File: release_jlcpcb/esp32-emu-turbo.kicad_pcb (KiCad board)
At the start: 4 copper layers, 160 x 75 mm, 71 parts, among them J1 USB-C-16P, J3 JST-PH-2P, J4 FPC-40P-0.5mm, SW1 SW-SMD-5.1x5.1, SW10 SW-SMD-5.1x5.1, SW11 SW-SMD-5.1x5.1, SW12 SW-SMD-5.1x5.1, SW13 SW-SMD-5.1x5.1, SW2 SW-SMD-5.1x5.1, SW3 SW-SMD-5.1x5.1, SW4 SW-SMD-5.1x5.1, SW5 SW-SMD-5.1x5.1, SW6 SW-SMD-5.1x5.1, SW7 SW-SMD-5.1x5.1, SW8 SW-SMD-5.1x5.1, SW9 SW-SMD-5.1x5.1, U1 ESP32-S3-WROOM-1-N16R8, U2 ESOP-8, U3 SOT-223, U5 SOP-16, U6 TF-01A

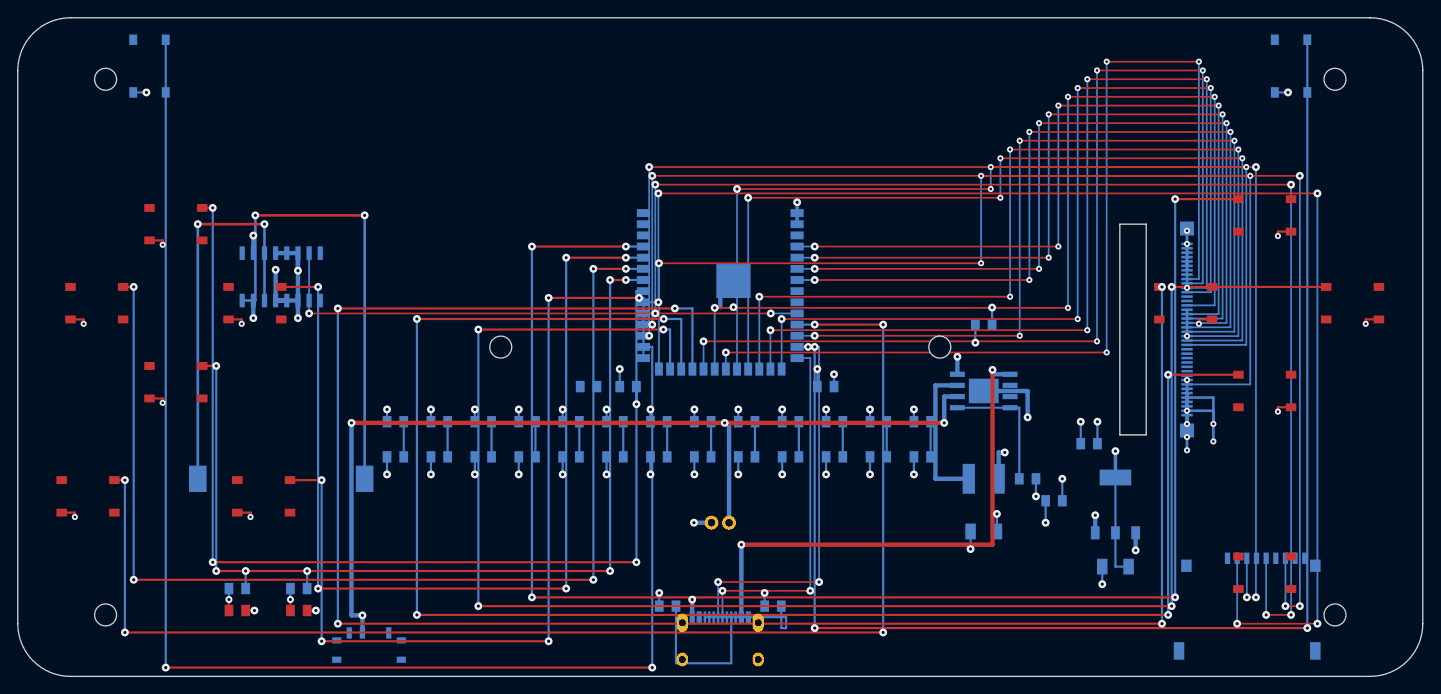
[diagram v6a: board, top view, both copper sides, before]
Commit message: Add JLCPCB DFM prevention: drill-trace + pad-net checks, pre-commit hook
Prevents two JLCPCB manufacturing review errors:
1. "The indicated hole will cut off the trace" — new drill-trace clearance test
2. "The pad and trace is connected" — pad net injection + trace-pad clearance test

Changes:
- routing.py: auto-capture pad-net mapping via _seg()/_via_net() endpoint matching
- board.py: inject correct net IDs into footprint pads (was net=0 for all)
- verify_dfm_v2.py: add _point_to_segment_dist(), test_drill_trace_clearance (42),
  test_trace_pad_different_net_clearance (43) with regression baselines
- pcb_cache.py: fix via net parsing regex (was broken, all vias showed net=0)
- drc_native.py: remove "shorting_items" from KNOWN_ACCEPTABLE (no longer needed)
- .git/hooks/pre-commit: run DFM verification on PCB file commits
- Regenerated PCB + gerbers + release_jlcpcb/ (43/43 DFM + 9/9 DFA pass)

Co-Authored-By: Claude Opus 4.6 <noreply@anthropic.com>
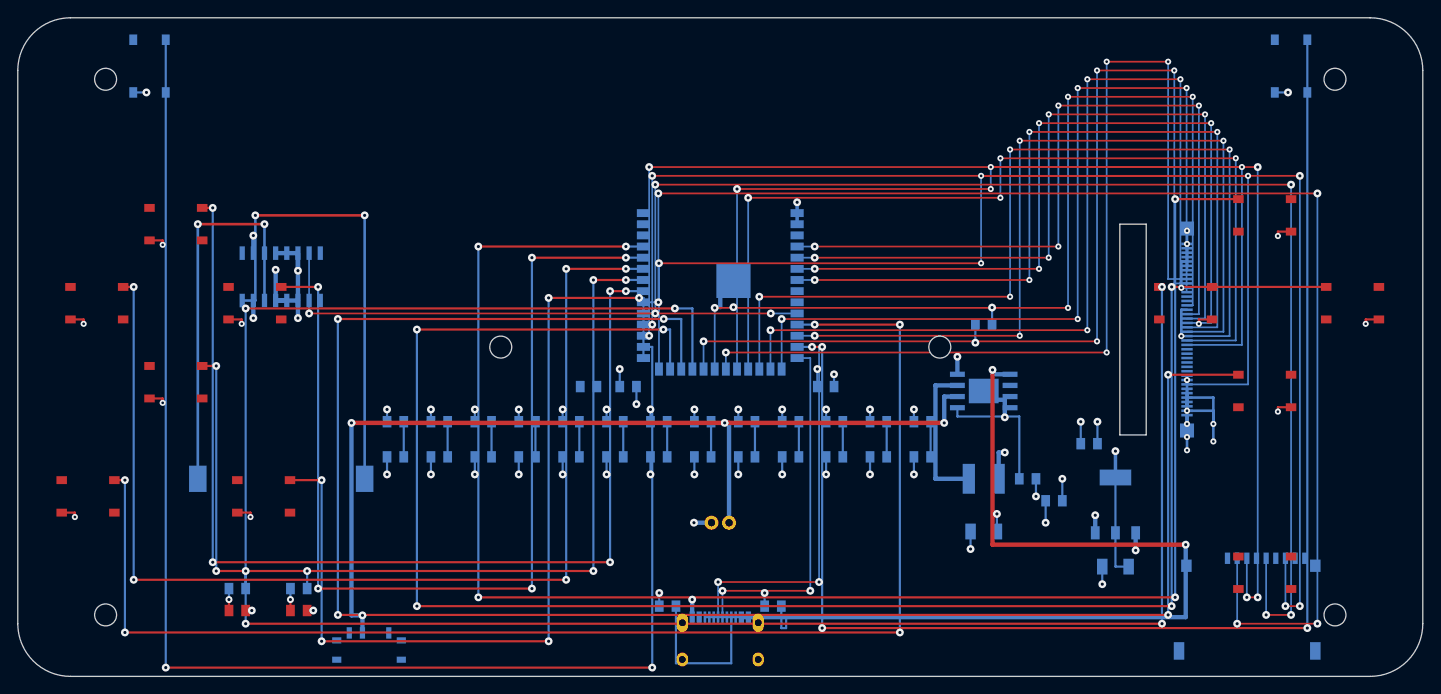
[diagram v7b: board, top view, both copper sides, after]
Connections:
- C1 pad 1: (no net) -> +5V
- C1 pad 2: (no net) -> GND
- C17 pad 1: (no net) -> VBUS
- C17 pad 2: (no net) -> GND
- C18 pad 1: (no net) -> BAT+
- C18 pad 2: (no net) -> GND
- C19 pad 1: (no net) -> +5V
- C19 pad 2: (no net) -> GND
- C2 pad 1: (no net) -> +3V3
- C2 pad 2: (no net) -> GND
- C3 pad 1: (no net) -> +3V3
- C3 pad 2: (no net) -> GND
- C4 pad 1: (no net) -> +3V3
- C4 pad 2: (no net) -> GND
- J1 pad A12: (no net) -> GND
- J1 pad A4: (no net) -> VBUS
- J1 pad A5: (no net) -> USB_CC1
- J1 pad A6: (no net) -> USB_D+
- J1 pad A7: (no net) -> USB_D-
- J1 pad B5: (no net) -> USB_CC2
- J3 pad 1: (no net) -> BAT+
- J3 pad 2: (no net) -> GND
- J4 pad 1: (no net) -> +3V3
- J4 pad 10: (no net) -> LCD_DC
- J4 pad 11: (no net) -> LCD_WR
- J4 pad 12: (no net) -> LCD_RD
- J4 pad 15: (no net) -> LCD_RST
- J4 pad 16: (no net) -> GND
- J4 pad 17: (no net) -> LCD_D0
- J4 pad 18: (no net) -> LCD_D1
- J4 pad 19: (no net) -> LCD_D2
- J4 pad 20: (no net) -> LCD_D3
- J4 pad 21: (no net) -> LCD_D4
- J4 pad 22: (no net) -> LCD_D5
- J4 pad 23: (no net) -> LCD_D6
- J4 pad 24: (no net) -> LCD_D7
- J4 pad 32: (no net) -> +3V3
- J4 pad 33: (no net) -> LCD_BL
- J4 pad 34: (no net) -> GND
- J4 pad 35: (no net) -> GND
- J4 pad 36: (no net) -> GND
- J4 pad 37: (no net) -> GND
- J4 pad 38: (no net) -> +3V3
- J4 pad 39: (no net) -> +3V3
- J4 pad 40: (no net) -> GND
- J4 pad 5: (no net) -> GND
- J4 pad 6: (no net) -> +3V3
- J4 pad 7: (no net) -> +3V3
- J4 pad 9: (no net) -> LCD_CS
- L1 pad 1: (no net) -> BAT+
- L1 pad 2: (no net) -> LX
- LED1 pad 2: (no net) -> GND
- LED2 pad 2: (no net) -> GND
- R1 pad 1: (no net) -> USB_CC1
- R1 pad 2: (no net) -> GND
- R16 pad 1: (no net) -> +5V
- R16 pad 2: (no net) -> IP5306_KEY
- R17 pad 1: (no net) -> +3V3
- R18 pad 1: (no net) -> +3V3
- R2 pad 1: (no net) -> USB_CC2
- R2 pad 2: (no net) -> GND
- SPK1 pad 1: (no net) -> SPK+
- SPK1 pad 2: (no net) -> SPK-
- SW1 pad 2: (no net) -> BTN_UP
- SW1 pad 3: (no net) -> GND
- SW10 pad 2: (no net) -> BTN_SELECT
- SW10 pad 3: (no net) -> GND
- SW11 pad 2: (no net) -> GND
- SW11 pad 3: (no net) -> BTN_L
- SW12 pad 2: (no net) -> GND
- SW12 pad 3: (no net) -> BTN_R
- SW2 pad 2: (no net) -> BTN_DOWN
- SW2 pad 3: (no net) -> GND
- SW3 pad 2: (no net) -> BTN_LEFT
- SW3 pad 3: (no net) -> GND
- SW4 pad 2: (no net) -> BTN_RIGHT
- SW4 pad 3: (no net) -> GND
- SW5 pad 1: (no net) -> BTN_A
- SW5 pad 4: (no net) -> GND
- SW6 pad 1: (no net) -> BTN_B
- SW6 pad 4: (no net) -> GND
- SW7 pad 1: (no net) -> BTN_X
- SW7 pad 4: (no net) -> GND
- SW8 pad 1: (no net) -> BTN_Y
- SW8 pad 4: (no net) -> GND
- SW9 pad 2: (no net) -> BTN_START
- SW9 pad 3: (no net) -> GND
- SW_PWR pad 2: (no net) -> BAT+
- U1 pad 10: (no net) -> I2S_DOUT
- U1 pad 11: (no net) -> BTN_START
- U1 pad 12: (no net) -> LCD_D4
- U1 pad 13: (no net) -> BTN_R
- U1 pad 14: (no net) -> USB_D+
- U1 pad 15: (no net) -> LCD_RD
- U1 pad 16: (no net) -> LCD_WR
- U1 pad 17: (no net) -> LCD_D5
- U1 pad 18: (no net) -> LCD_D6
- U1 pad 19: (no net) -> LCD_D7
- U1 pad 2: (no net) -> +3V3
- U1 pad 20: (no net) -> LCD_CS
- U1 pad 21: (no net) -> LCD_RST
- U1 pad 22: (no net) -> LCD_DC
- U1 pad 23: (no net) -> BTN_Y
- U1 pad 24: (no net) -> BTN_X
- U1 pad 25: (no net) -> BTN_B
- U1 pad 26: (no net) -> LCD_BL
- U1 pad 27: (no net) -> BTN_SELECT
- U1 pad 28: (no net) -> BTN_L
- U1 pad 29: (no net) -> SD_MOSI
- U1 pad 30: (no net) -> SD_MISO
- U1 pad 31: (no net) -> SD_CLK
- U1 pad 32: (no net) -> SD_CS
- U1 pad 33: (no net) -> BTN_UP
- U1 pad 34: (no net) -> BTN_DOWN
- U1 pad 35: (no net) -> BTN_LEFT
- U1 pad 36: (no net) -> BTN_RIGHT
- U1 pad 37: (no net) -> BTN_A
- U1 pad 4: (no net) -> LCD_D0
- U1 pad 41: (no net) -> GND
- U1 pad 5: (no net) -> LCD_D1
- U1 pad 6: (no net) -> LCD_D2
- U1 pad 7: (no net) -> LCD_D3
- U2 pad 1: (no net) -> VBUS
- U2 pad 5: (no net) -> IP5306_KEY
- U2 pad 6: (no net) -> BAT+
- U2 pad 7: (no net) -> LX
- U2 pad 8: (no net) -> +5V
- U2 pad EP: (no net) -> GND
- U3 pad 1: (no net) -> GND
- U3 pad 3: (no net) -> +5V
- U3 pad 4: (no net) -> +3V3
- U5 pad 10: (no net) -> I2S_DOUT
- U5 pad 11: (no net) -> GND
- U5 pad 12: (no net) -> +5V
- U5 pad 13: (no net) -> +5V
- U5 pad 14: (no net) -> SPK-
- U5 pad 15: (no net) -> GND
- U5 pad 16: (no net) -> SPK+
- U5 pad 2: (no net) -> GND
- U5 pad 4: (no net) -> +5V
- U5 pad 5: (no net) -> +5V
- U5 pad 6: (no net) -> +5V
- U5 pad 7: (no net) -> I2S_DOUT
- U6 pad 2: (no net) -> SD_CS
- U6 pad 3: (no net) -> SD_MOSI
- U6 pad 5: (no net) -> SD_CLK
- U6 pad 7: (no net) -> SD_MISO
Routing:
- net VBUS: track 61.3 -> 105.3 mm
- net BTN_Y: track 219.7 -> 240.7 mm
- net BTN_X: track 194.4 -> 212.4 mm
- net BTN_B: track 194.7 -> 208.7 mm
- net BTN_A: track 182.5 -> 194.7 mm
- net LCD_RD: track 106.8 -> 101.4 mm
- net LCD_RST: track 114.8 -> 109.8 mm
- net LCD_WR: track 108.7 -> 104.2 mm
- net LCD_D0: track 91.4 -> 86.9 mm
- net LCD_D1: track 92.1 -> 88.1 mm
- net BTN_START: track 153.8 -> 157.6 mm
- net LCD_DC: track 116.9 -> 113.3 mm
- net LCD_D2: track 92.7 -> 89.2 mm
- net LCD_D3: track 93.4 -> 90.4 mm
- net LCD_CS: track 115.0 -> 112.3 mm
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
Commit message: Fix PAM8403 copper-to-copper clearance violations, tighten DFM baselines
Routing fixes (routing.py):
- SPK+ (net42) exit U5:16 LEFTWARD (col_x=24.5) instead of right (+1.5mm).
  Old route at x=27.055 passed through U5:15 (GND pad, gap=-0.65mm) and
  U5:2 (GND pad, gap=-0.22mm). New route clears all U5 pads by >=0.605mm.
- Replace +5V bridge (VDD6→PVDD13 via x=31.905) with direct PVDD4→PVDD13
  vertical (x=29.365). Old bridge crossed U5:11 GND pad (gap=-0.45mm).
  New vert only touches same-net (+5V) pads U5:4 and U5:13.

Result: 157 -> 147 collision grid violations (-10). 43/43 DFM tests pass.

DFM baseline updates (verify_dfm_v2.py):
- Trace-to-pad baseline: 140 -> 106 (reflecting actual cleared violations)
- Drill-to-trace baseline: 71 -> 45

Release: gerbers, BOM, CPL, .kicad_pcb updated in release_jlcpcb/.

Co-Authored-By: Claude Opus 4.6 <noreply@anthropic.com>
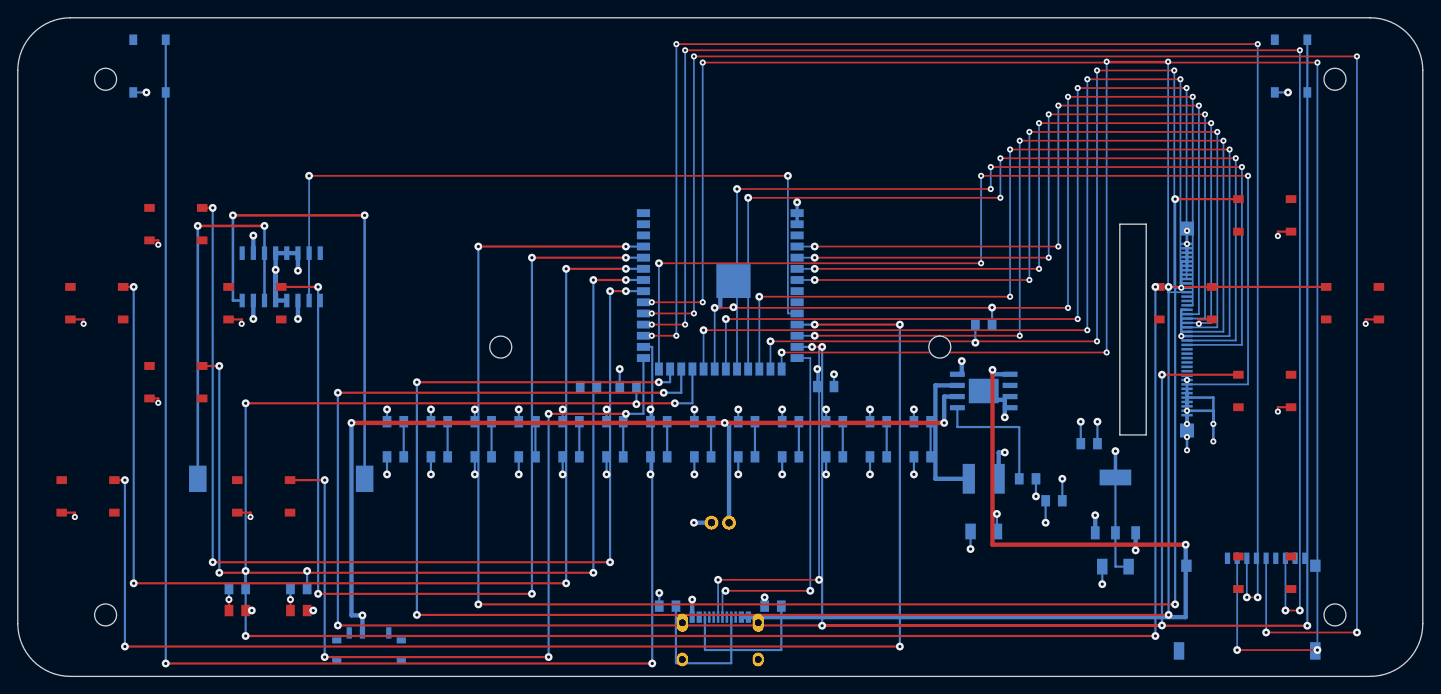
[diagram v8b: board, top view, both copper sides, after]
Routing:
- net SD_CLK: track 146.7 -> 194.9 mm, vias 5 -> 6
- net SD_CS: track 154.7 -> 190.5 mm, vias 5 -> 6
- net SD_MISO: track 147.8 -> 177.4 mm, vias 5 -> 6
- net I2S_DOUT: track 62.4 -> 90.8 mm
- net SD_MOSI: track 143.8 -> 171.8 mm, vias 5 -> 6
- net BTN_Y: track 240.7 -> 229.1 mm
- net BTN_SELECT: track 108.6 -> 98.4 mm
- net BTN_X: track 212.4 -> 203.4 mm
- net BTN_B: track 208.7 -> 201.7 mm
- net LCD_RD: track 101.4 -> 107.4 mm
- net LCD_CS: track 112.3 -> 106.3 mm
- net USB_CC2: track 13.6 -> 17.4 mm
- net BTN_START: track 157.6 -> 160.8 mm
- net +5V: track 27.8 -> 25.2 mm
- net SPK+: track 53.6 -> 55.8 mm
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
